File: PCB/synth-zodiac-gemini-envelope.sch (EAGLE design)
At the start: 59 parts, among them Q1 PMP4201, U3 LM393, U4 TL074A, U5 CD4066

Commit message: Snapshot of designs so far.
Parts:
- removed BIAS: NP, rlc:TRIMPOTTC33X
- removed C10: 220pF, rlc:CAPACITOR0603
- removed C5: 3900pF, rlc:CAPACITOR0603
- removed C6, C7: 0.1uF, rlc:CAPACITOR0603
- removed C8: 1.0uF, rlc:CAPACITOR0603
- removed C9: 100pF, rlc:CAPACITOR0603
- removed CP_EXP_VCO, CP_GND, CP_VCO_LIN_FM, CP_VCO_OUT: PADSMD-070X070, con-testpoints:PADSMD-070X070
- removed EXP_VCO_TRIM: 100K - NP, rlc:TRIMPOTTC33X
- removed FREQ: 10K, rlc:TRIMPOT9MM_PCB_SHAFT
- removed GLYPH: Aquarius, circuit-monkey-zodiac:GLYPH-AQUARIUS
- removed J1: (no value), con-jst:04P-VT-SMT
- removed KB_CV, PWM_CV, VCO_MOD_CV, VCO_OUT: 2-pin, VT, SMT, con-jst:02PVT-SMT
- removed KB_TRIM: 100K, rlc:TRIMPOTTC33X
- removed PCB: PCB FAB, circuit-monkey-zodiac:PENTAGON-40R
- removed PULSE, SAW, TP4: TPSMD-040-RND, con-testpoints:TPSMD-040-RND
- removed R10, R11, R13, R14, R24: 0, rlc:RESISTOR0603
- removed R12: NS, rlc:RESISTOR0603
- removed R15, R16: 100K, rlc:RESISTOR0603
- removed R17: 10.0K, rlc:RESISTOR0603
- removed R18: 4.75M, rlc:RESISTOR0603
- removed R19, R20, R21, R22: 4.99K, rlc:RESISTOR0603
- removed R23, R9: 10K, rlc:RESISTOR0603
- removed R4: 412K, rlc:RESISTOR0603
- removed R5: 68.1K - NP, rlc:RESISTOR0603
- removed R6: 2.2K, rlc:RESISTOR0603
- removed R7: 499K, rlc:RESISTOR0603
- removed R8: 1.82M, rlc:RESISTOR0603
- removed TYPE: SPDT, switch-thd:SLIDE-SPDTSS-12-F45-TH-PCB
- removed U3: LM393, op-amp:DUAL-LM393ED
- removed U4: TL074A, op-amp:QUADTL074A-SOIC
- removed U5: CD4066, logic:CD4066SO14
- added ATTACK, DECAY: 1M, rlc:TRIMPOT9MM_PCB_SHAFT
- added EG_VCA, EG_VCF_MOD, EG_VCO_MOD, GATE, TRIG: 2-pin, VT, SMT, con-jst:02PVT-SMT
- added GLYPH1: Gemini, circuit-monkey-zodiac:GLYPH-GEMINI
- added PCB1: PCB FAB, circuit-monkey-zodiac:PENTAGON-40R
- added PWR_IN, PWR_LFO, PWR_VCF, PWR_VCF_MOD, PWR_VCO, PWR_VCO_MOD: (no value), con-jst:04P-VT-SMT
- added R1: 1.00M, rlc:RESISTOR0603
- added SUST: SPDT, switch-thd:SLIDE-SPDTSS-12-F45-TH-PCB
- added U1: TL074A, op-amp:QUADTL074A-SOIC
- C1: value 4700pF -> 1.0uF
- C2: value 22uF -> 2.2uF
- CONST1: value Aquarius -> Gemini; device circuit-monkey-zodiac:CONSTELLATION-AQUARIUS -> circuit-monkey-zodiac:CONSTELLATION-GEMINI
- Q1: value PMP4201 -> PNP; device transistor-bjt:NPN-DUALPMP4201 -> transistor-bjt:PNP-BC856
- R2: value 221K -> 1.00M
- R3: value 221K -> 100K
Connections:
- removed net BIAS: BIAS.2, R19.2, R20.1, R21.1
- removed net EXP_VCO_CV_IN: CP_EXP_VCO.PAD, EXP_VCO_TRIM.1
- removed net EXP_VCO_LIN_FM: CP_VCO_LIN_FM.PAD, R7.1
- removed net FREQ: FREQ.2, R2.1
- removed net FREQ_CV_MIX: C1.1, R2.2, R3.2, R4.2, R5.2, R6.1, U4-A.-
- removed net KB_CV: KB_CV.1, KB_TRIM.1
- removed net N$12: Q1-A.EMITTER, R7.2, R8.2, U4-B.+
- removed net N$13: Q1-B.EMITTER, U4-B.-, U4-B.OUT
- removed net N$14: C1.2, Q1-A.BASE, R6.2, U4-A.OUT
- removed net N$15: R12.2, R9.2, U5-A.EN, U5-B.EN, U5-C.IN
- removed net N$16: C9.1, R17.1, R18.1, U4-D.+
- removed net N$17: R14.2, U3-B.-
- removed net N$18: C9.2, D1.A, R18.2, U4-D.OUT
- removed net N$20: C5.2, Q1-B.COLLECTOR, U4-C.+, U5-A.OUT
- removed net N$21: BIAS.3, C8.2, R17.2, R19.1
- removed net N$22: C10.1, R21.2, U5-B.IN
- removed net N$23: R12.1, U5-D.OUT
- removed net N$24: D1.K, D2.K, R23.1, U5-C.EN
- removed net N$25: R10.2, U5-D.IN
- removed net N$26: R11.2, U5-D.EN
- removed net N$27: R13.2, U3-B.+
- removed net N$28: R15.2, R16.1, U3-A.-
- removed net N$29: TP4.P$1, U3-B.OUT
- removed net N$8: KB_TRIM.2, KB_TRIM.3, R4.1
- removed net N$9: EXP_VCO_TRIM.2, EXP_VCO_TRIM.3, R5.1
- removed net PULSE: PULSE.P$1, R22.2, TYPE-SW.B, U3-A.OUT
- removed net PWM_CV: PWM_CV.1, R15.1
- removed net SAW: R24.2, TYPE-SW.A
- removed net VCO_CORE: R24.1, SAW.P$1, U3-A.+, U4-C.-, U4-C.OUT, U4-D.-
- removed net VCO_MOD_CV: R3.1, VCO_MOD_CV.1
- removed net VCO_OUT: CP_VCO_OUT.PAD, TYPE-SW.C, VCO_OUT.1
- new net EG: EG_VCF_MOD.1, EG_VCO_MOD.1, Q1.BASE, U1-A.-, U1-A.OUT
- new net EG_VCA: EG_VCA.1, U1-C.-, U1-C.OUT
- new net GATE: GATE.1, SUST-SW.B
- new net N$134: R1.2, SUST-SW.C, U1-B.+
- new net N$136: ATTACK.1, D1.K, U1-B.OUT
- new net N$137: ATTACK.2, ATTACK.3, C1.1, D1.A, U1-D.+
- new net N$138: C2.1, D2.K, DECAY.2, DECAY.3, U1-A.+
- new net N$139: D2.A, DECAY.1, R2.2, U1-B.-, U1-D.-, U1-D.OUT
- new net N$140: Q1.COLLECTOR, R3.1, U1-C.+
- new net TRIG: SUST-SW.A, TRIG.1
- net +5V: now also PWR_IN.3, PWR_LFO.3, PWR_VCF.3, PWR_VCF_MOD.3, PWR_VCO.3, PWR_VCO_MOD.3; no longer C2.2, C5.1, J1.3, R16.2, R22.1, U5-A.IN
- net +9V: now also C3.1, PWR_IN.1, PWR_LFO.1, PWR_VCF.1, PWR_VCF_MOD.1, PWR_VCO.1, PWR_VCO_MOD.1, R3.2, U1-PWR.V+; no longer C10.2, C3.2, C6.2, C7.2, FREQ.3, J1.1, U3-PWR.V+, U4-PWR.V+, U5-B.OUT, U5-C.OUT, U5-PWR.VCC
- net -9V: now also C4.2, PWR_IN.2, PWR_LFO.2, PWR_VCF.2, PWR_VCF_MOD.2, PWR_VCO.2, PWR_VCO_MOD.2, U1-PWR.V-; no longer C4.1, FREQ.1, J1.2, R8.1, U4-PWR.V-
- net GND: now also C1.2, C2.2, C3.2, C4.1, EG_VCA.2, EG_VCF_MOD.2, EG_VCO_MOD.2, GATE.2, PCB1.GND@1, PWR_IN.4, PWR_LFO.4, PWR_VCF.4, PWR_VCF_MOD.4, PWR_VCO.4, PWR_VCO_MOD.4, Q1.EMITTER, R1.1, R2.1, SUST-MTG.MT1, SUST-MTG.MT2, TRIG.2; no longer BIAS.1, C2.1, C3.1, C4.2, C6.1, C7.1, C8.1, CP_GND.PAD, D2.A, J1.4, KB_CV.2, PCB.GND@1, PWM_CV.2, Q1-A.COLLECTOR, Q1-B.BASE, R10.1, R11.1, R13.1, R14.1, R20.2, R23.2, R9.1, TYPE-MTG.MT1, TYPE-MTG.MT2, U3-PWR.V-, U4-A.+, U5-PWR.GND, VCO_MOD_CV.2, VCO_OUT.2
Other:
- note added: "==> VCA"
- note added: "==> VCF MOD"
- note added: "==> VCO MOD"
- note added: "ENVELOPE GENERATOR (EG)"
- note removed: "=> VCF / CV_PNL"
- note removed: "Aquarius"
- note removed: "CP =>"
- note removed: "KB =>"
- note removed: "PULSE"
- note removed: "SAW"
- note removed: "VCO"
- note removed: "VCO FREQ"
- note removed: "VCO WAVE"
- note removed: "VCO_MOD =>"
- note removed: "Zodiac Synth"
- moved on the sheet: C1, C2, C3, C4, CONST1, D1, D2, R2, R3

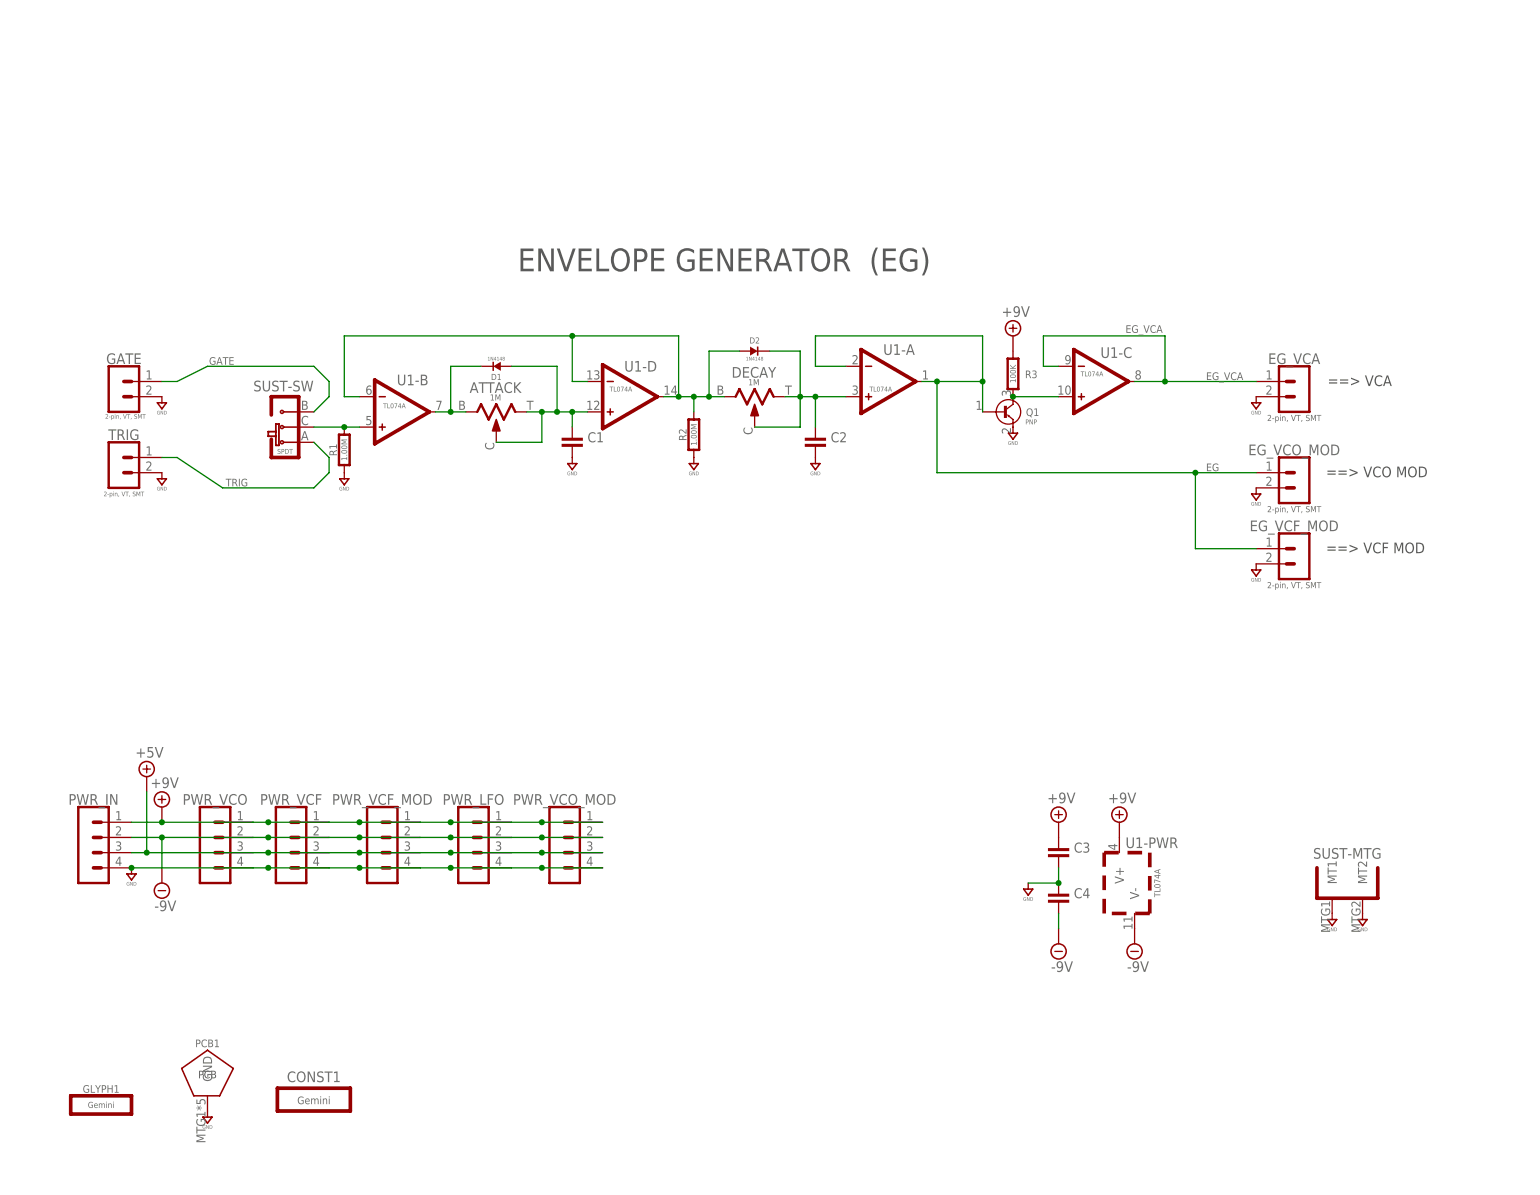
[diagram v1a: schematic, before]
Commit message: Almost ready for FAB.
Sagittarius was mis-spelled, renamed it.  Taurus is still WIP.
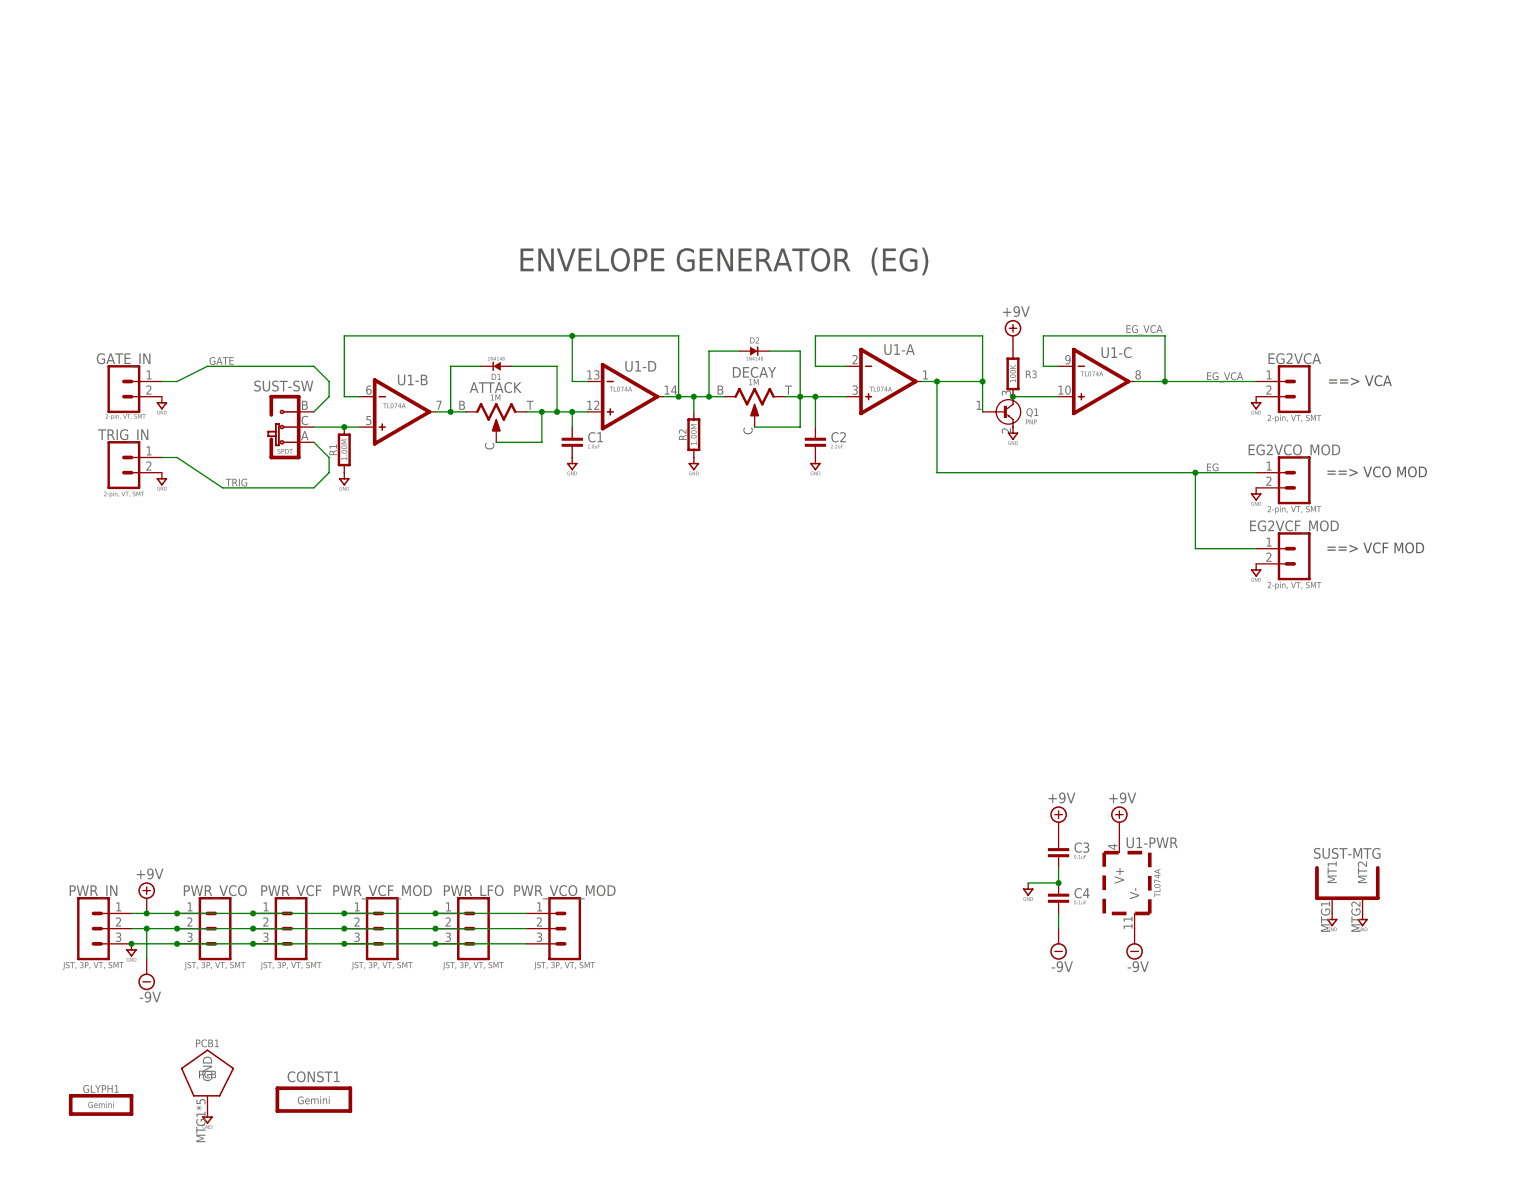
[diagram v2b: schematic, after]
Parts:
- PWR_IN, PWR_LFO, PWR_VCF, PWR_VCF_MOD, PWR_VCO, PWR_VCO_MOD: value (none) -> JST, 3P, VT, SMT; device con-jst:04P-VT-SMT -> con-jst:03P-VT-SMT
- renumbered EG_VCA to EG2VCA, EG_VCF_MOD to EG2VCF_MOD, EG_VCO_MOD to EG2VCO_MOD, GATE to GATE_IN, TRIG to TRIG_IN
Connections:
- removed net +5V: PWR_IN.3, PWR_LFO.3, PWR_VCF.3, PWR_VCF_MOD.3, PWR_VCO.3, PWR_VCO_MOD.3
- net GND: now also PWR_IN.3, PWR_LFO.3, PWR_VCF.3, PWR_VCF_MOD.3, PWR_VCO.3, PWR_VCO_MOD.3; no longer PWR_IN.4, PWR_LFO.4, PWR_VCF.4, PWR_VCF_MOD.4, PWR_VCO.4, PWR_VCO_MOD.4

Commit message: Work in progress for rev A,  VCO rev.B
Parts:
- removed EG2VCF_MOD, EG2VCO_MOD: 2-pin, VT, SMT, con-jst:02PVT-SMT
- removed PWR_LFO, PWR_VCF, PWR_VCF_MOD, PWR_VCO, PWR_VCO_MOD: JST, 3P, VT, SMT, con-jst:03P-VT-SMT
- removed SUST: SPDT, switch-thd:SLIDE-SPDTSS-12-F45-TH-PCB
- added EG2VCFMOD, EG2VCOMOD: JST, SH, 2P, con-jst:02P-SM-VT-SMT
- added SRC: (no value), switch-thd:SLIDE-SPDT-MNTSS-12-F45-TH-PCB
- EG2VCA, GATE_IN, TRIG_IN: value 2-pin, VT, SMT -> JST, SH, 2P; device con-jst:02PVT-SMT -> con-jst:02P-SM-VT-SMT
- PWR_IN: value JST, 3P, VT, SMT -> JST SM 3P; device con-jst:03P-VT-SMT -> con-jst:03P-SM-VT-SMT
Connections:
- net +9V: no longer PWR_LFO.1, PWR_VCF.1, PWR_VCF_MOD.1, PWR_VCO.1, PWR_VCO_MOD.1
- net -9V: no longer PWR_LFO.2, PWR_VCF.2, PWR_VCF_MOD.2, PWR_VCO.2, PWR_VCO_MOD.2
- net EG: now also EG2VCFMOD.1, EG2VCOMOD.1; no longer EG2VCF_MOD.1, EG2VCO_MOD.1
- net GATE: now also SRC-SW.B; no longer SUST-SW.B
- net GND: now also EG2VCFMOD.2, EG2VCOMOD.2, SRC-MTG.MT1, SRC-MTG.MT2; no longer EG2VCF_MOD.2, EG2VCO_MOD.2, PWR_LFO.3, PWR_VCF.3, PWR_VCF_MOD.3, PWR_VCO.3, PWR_VCO_MOD.3, SUST-MTG.MT1, SUST-MTG.MT2
- net N$134: now also SRC-SW.C; no longer SUST-SW.C
- net TRIG: now also SRC-SW.A; no longer SUST-SW.A
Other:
- note added: "EG"
- note added: "Gemini"
- note added: "KBD==>"
- note added: "SATAN'S CYCLE WORKS"
- note added: "Zodiac Synth"
- moved on the sheet: PWR_IN

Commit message: Perhaps final Rev. A?
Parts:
- SRC: device switch-thd:SLIDE-SPDT-MNTSS-12-F45-TH-PCB -> switch-thd:SLIDE-SPDT-MNTSS-12-F45-TH-PCB-2
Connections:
- net GATE: now also SRC-SW.A; no longer SRC-SW.B
- net TRIG: now also SRC-SW.B; no longer SRC-SW.A
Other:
- moved on the sheet: SRC-MTG, SRC-SW
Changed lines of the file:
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@@
 <part name="EG2VCFMOD" library="con-jst" library_urn="urn:adsk.eagle:library:7191852" deviceset="02P" device="-SM-VT-SMT" package3d_urn="urn:adsk.eagle:package:41368283/6" value="JST, SH, 2P"/>
 <part name="PWR_IN" library="con-jst" library_urn="urn:adsk.eagle:library:7191852" deviceset="03P" device="-SM-VT-SMT" package3d_urn="urn:adsk.eagle:package:41368284/5" value="JST SM 3P"/>
-<part name="SRC" library="switch-thd" library_urn="urn:adsk.eagle:library:26242324" deviceset="SLIDE-SPDT-MNT" device="SS-12-F45-TH-PCB" package3d_urn="urn:adsk.eagle:package:36475164/3"/>
+<part name="SRC" library="switch-thd" library_urn="urn:adsk.eagle:library:26242324" deviceset="SLIDE-SPDT-MNT" device="SS-12-F45-TH-PCB-2"/>
 </parts>
 <sheets>
@@
 <attribute name="NAME" x="8.89" y="44.45" size="1.778" layer="95" font="vector" ratio="15" align="center"/>
 </instance>
-<instance part="SRC" gate="-SW" x="43.18" y="121.92" smashed="yes" rot="R90">
-<attribute name="NAME" x="39.116" y="121.92" size="1.778" layer="95" ratio="15" rot="R90" align="center"/>
-<attribute name="VALUE" x="37.592" y="122.174" size="0.8128" layer="96" rot="R90" align="center"/>
+<instance part="SRC" gate="-SW" x="43.18" y="121.92" smashed="yes" rot="MR270">
+<attribute name="NAME" x="39.116" y="121.92" size="1.778" layer="95" ratio="15" rot="MR270" align="center"/>
+<attribute name="VALUE" x="37.592" y="121.666" size="0.8128" layer="96" rot="MR270" align="center"/>
 </instance>
 <instance part="SRC" gate="-MTG" x="218.44" y="45.72" smashed="yes">
@@
 <wire x1="48.26" y1="132.08" x2="50.8" y2="129.54" width="0.1524" layer="91"/>
 <wire x1="50.8" y1="129.54" x2="50.8" y2="127" width="0.1524" layer="91"/>
+<pinref part="GATE_IN" gate="G$1" pin="1"/>
+<pinref part="SRC" gate="-SW" pin="A"/>
 <wire x1="50.8" y1="127" x2="48.26" y2="124.46" width="0.1524" layer="91"/>
-<pinref part="GATE_IN" gate="G$1" pin="1"/>
-<pinref part="SRC" gate="-SW" pin="B"/>
 </segment>
 </net>
@@
 <wire x1="48.26" y1="111.76" x2="50.8" y2="114.3" width="0.1524" layer="91"/>
 <wire x1="50.8" y1="114.3" x2="50.8" y2="116.84" width="0.1524" layer="91"/>
-<wire x1="50.8" y1="116.84" x2="48.26" y2="119.38" width="0.1524" layer="91"/>
 <pinref part="TRIG_IN" gate="G$1" pin="1"/>
-<pinref part="SRC" gate="-SW" pin="A"/>
-</segment>
-</net>
+<pinref part="SRC" gate="-SW" pin="B"/>
+<wire x1="48.26" y1="119.38" x2="50.8" y2="116.84" width="0.1524" layer="91"/>
+</segment>
+</net>
